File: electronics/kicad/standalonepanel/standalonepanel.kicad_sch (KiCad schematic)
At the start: 106 parts, among them J1 LEDPWR, J2 USB_C-PD, J3 Speaker, Q1 AO4435, SW1 SET, SW2 BOOT, SW3 UP, SW4 DOWN, SW5 TST-ICE40, SW6 RESET, U1 SC189ZSKTRT, U10 DS3231, U2 SC189CSKTRT, U3 CH340C, U4 ESP32-WROVER-E, U5 IS64WV25616EFBLL-10TLI, U6 STUSB4500QTR, U7 ICE40-HX4K, U8 MAX98357A, U9 MPU-6050, X1 12MHz

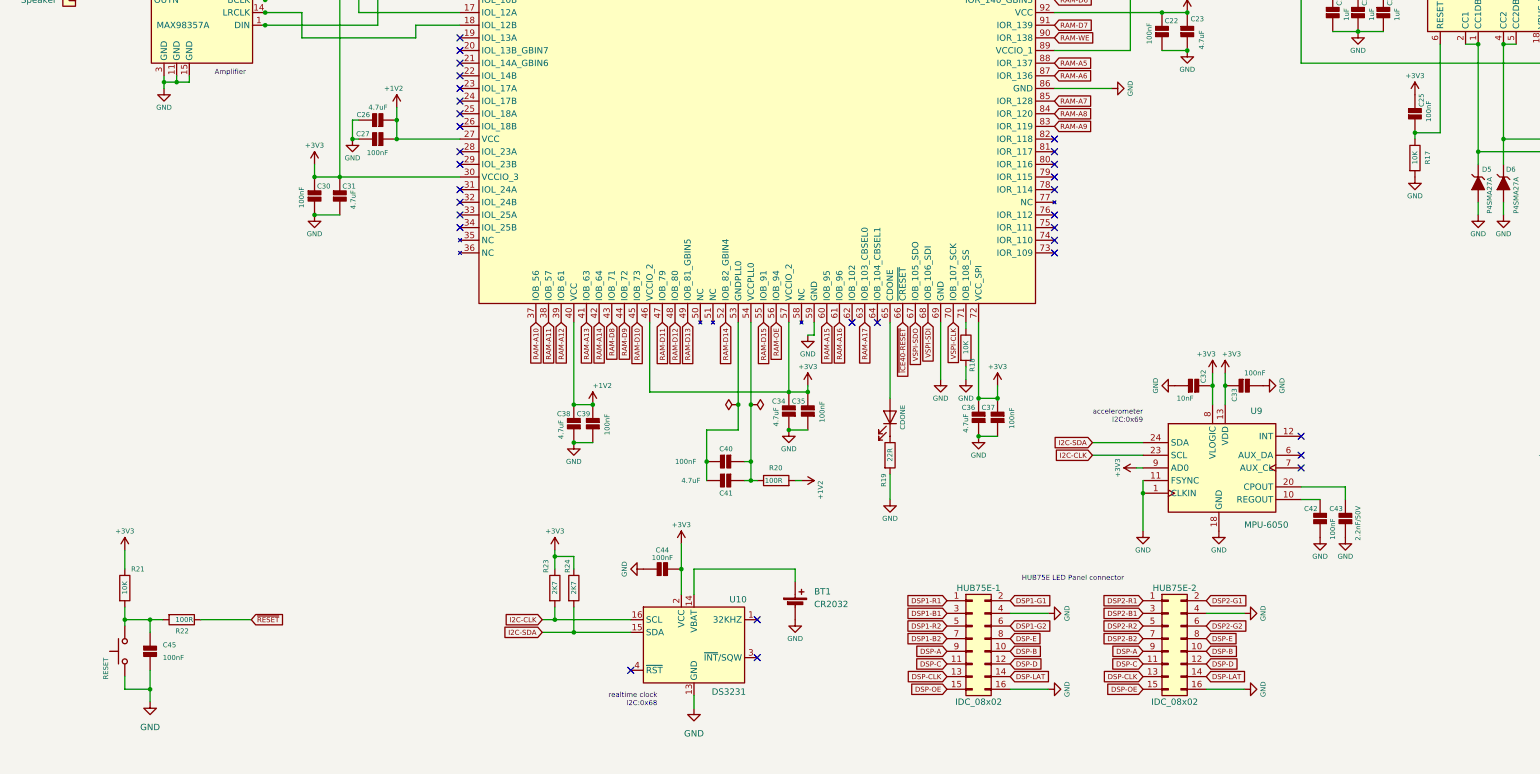
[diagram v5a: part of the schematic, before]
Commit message: added repeat of config selection
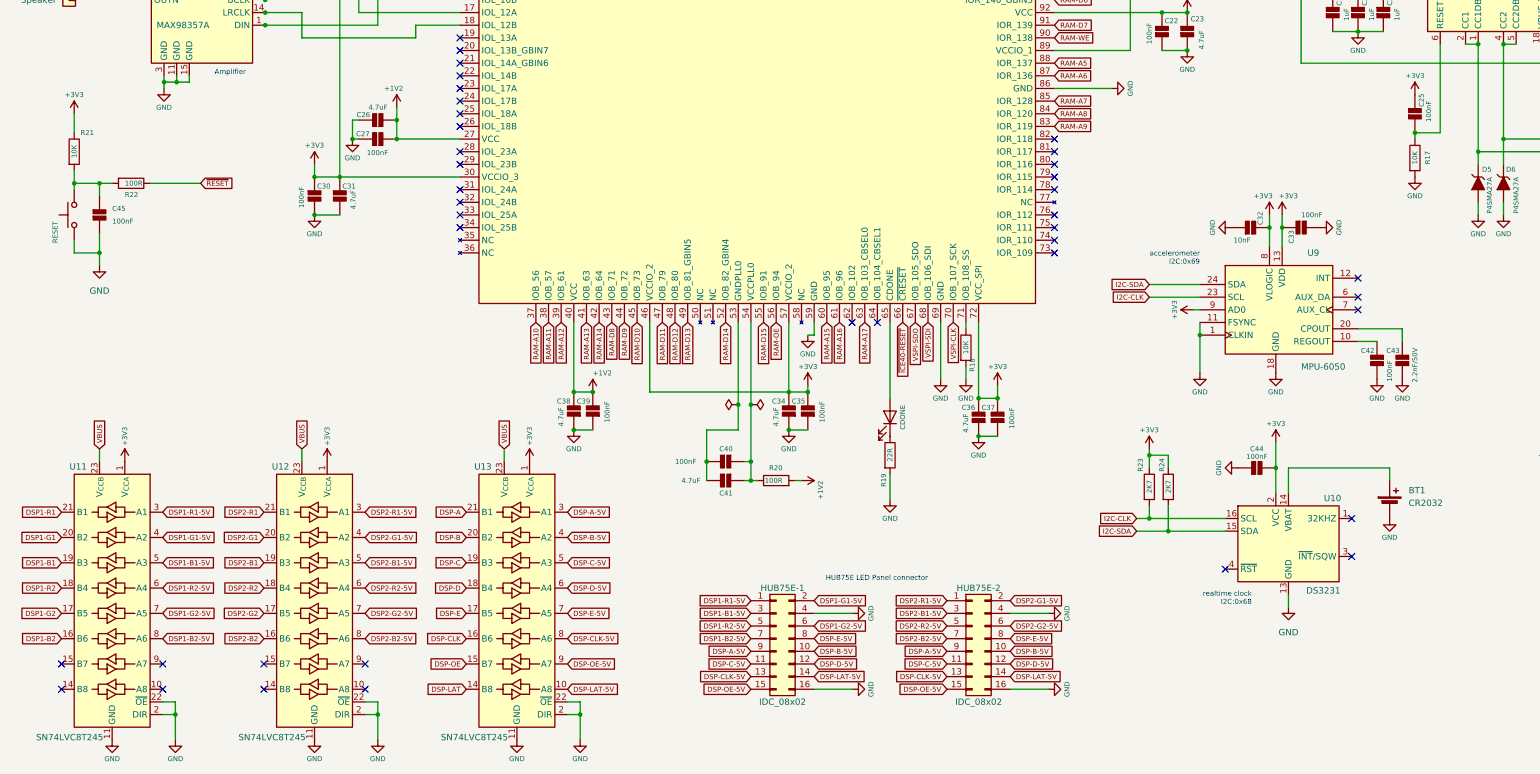
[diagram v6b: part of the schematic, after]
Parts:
- added U11, U12, U13: SN74LVC8T245, Package_SO:TSSOP-24_4.4x7.8mm_P0.65mm, symbol Logic_LevelTranslator:SN74LVC8T245
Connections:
- net +3V3: now also U11.1 (V_{CCA}), U12.1 (V_{CCA}), U13.1 (V_{CCA})
- net DSP-A: now also U13.21 (B1); no longer HUB75E-1.9 (Pin_9), HUB75E-2.9 (Pin_9)
- net DSP-B: now also U13.20 (B2); no longer HUB75E-1.10 (Pin_10), HUB75E-2.10 (Pin_10)
- net DSP-C: now also U13.19 (B3); no longer HUB75E-1.11 (Pin_11), HUB75E-2.11 (Pin_11)
- net DSP-CLK: now also U13.16 (B6); no longer HUB75E-1.13 (Pin_13), HUB75E-2.13 (Pin_13)
- net DSP-D: now also U13.18 (B4); no longer HUB75E-1.12 (Pin_12), HUB75E-2.12 (Pin_12)
- net DSP-E: now also U13.17 (B5); no longer HUB75E-1.8 (Pin_8), HUB75E-2.8 (Pin_8)
- net DSP-LAT: now also U13.14 (B8); no longer HUB75E-1.14 (Pin_14), HUB75E-2.14 (Pin_14)
- net DSP-OE: now also U13.15 (B7); no longer HUB75E-1.15 (Pin_15), HUB75E-2.15 (Pin_15)
- net DSP1-B1: now also U11.19 (B3); no longer HUB75E-1.3 (Pin_3)
- net DSP1-B2: now also U11.16 (B6); no longer HUB75E-1.7 (Pin_7)
- net DSP1-G1: now also U11.20 (B2); no longer HUB75E-1.2 (Pin_2)
- net DSP1-G2: now also U11.17 (B5); no longer HUB75E-1.6 (Pin_6)
- net DSP1-R1: now also U11.21 (B1); no longer HUB75E-1.1 (Pin_1)
- net DSP1-R2: now also U11.18 (B4); no longer HUB75E-1.5 (Pin_5)
- net DSP2-B1: now also U12.19 (B3); no longer HUB75E-2.3 (Pin_3)
- net DSP2-B2: now also U12.16 (B6); no longer HUB75E-2.7 (Pin_7)
- net DSP2-G1: now also U12.20 (B2); no longer HUB75E-2.2 (Pin_2)
- net DSP2-G2: now also U12.17 (B5); no longer HUB75E-2.6 (Pin_6)
- net DSP2-R1: now also U12.21 (B1); no longer HUB75E-2.1 (Pin_1)
- net DSP2-R2: now also U12.18 (B4); no longer HUB75E-2.5 (Pin_5)
- net GND: now also U11.11 (GND), U11.12 (GND), U11.13 (GND), U11.2 (DIR), U11.22 (~{OE}), U12.11 (GND), U12.12 (GND), U12.13 (GND), U12.2 (DIR), U12.22 (~{OE}), U13.11 (GND), U13.12 (GND), U13.13 (GND), U13.2 (DIR), U13.22 (~{OE})
- net VBUS: now also U11.23 (V_{CCB}), U11.24 (V_{CCB}), U12.23 (V_{CCB}), U12.24 (V_{CCB}), U13.23 (V_{CCB}), U13.24 (V_{CCB})
- new net DSP-A-5V: HUB75E-1.9 (Pin_9), HUB75E-2.9 (Pin_9), U13.3 (A1)
- new net DSP-B-5V: HUB75E-1.10 (Pin_10), HUB75E-2.10 (Pin_10), U13.4 (A2)
- new net DSP-C-5V: HUB75E-1.11 (Pin_11), HUB75E-2.11 (Pin_11), U13.5 (A3)
- new net DSP-CLK-5V: HUB75E-1.13 (Pin_13), HUB75E-2.13 (Pin_13), U13.8 (A6)
- new net DSP-D-5V: HUB75E-1.12 (Pin_12), HUB75E-2.12 (Pin_12), U13.6 (A4)
- new net DSP-E-5V: HUB75E-1.8 (Pin_8), HUB75E-2.8 (Pin_8), U13.7 (A5)
- new net DSP-LAT-5V: HUB75E-1.14 (Pin_14), HUB75E-2.14 (Pin_14), U13.10 (A8)
- new net DSP-OE-5V: HUB75E-1.15 (Pin_15), HUB75E-2.15 (Pin_15), U13.9 (A7)
- new net DSP1-B1-5V: HUB75E-1.3 (Pin_3), U11.5 (A3)
- new net DSP1-B2-5V: HUB75E-1.7 (Pin_7), U11.8 (A6)
- new net DSP1-G1-5V: HUB75E-1.2 (Pin_2), U11.4 (A2)
- new net DSP1-G2-5V: HUB75E-1.6 (Pin_6), U11.7 (A5)
- new net DSP1-R1-5V: HUB75E-1.1 (Pin_1), U11.3 (A1)
- new net DSP1-R2-5V: HUB75E-1.5 (Pin_5), U11.6 (A4)
- new net DSP2-B1-5V: HUB75E-2.3 (Pin_3), U12.5 (A3)
- new net DSP2-B2-5V: HUB75E-2.7 (Pin_7), U12.8 (A6)
- new net DSP2-G1-5V: HUB75E-2.2 (Pin_2), U12.4 (A2)
- new net DSP2-G2-5V: HUB75E-2.6 (Pin_6), U12.7 (A5)
- new net DSP2-R1-5V: HUB75E-2.1 (Pin_1), U12.3 (A1)
- new net DSP2-R2-5V: HUB75E-2.5 (Pin_5), U12.6 (A4)
- no-connect marks 78 -> 86
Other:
- moved on the sheet: BT1, C32, C33, C38, C39, C42, C43, C44, C45, HUB75E-1, HUB75E-2, R21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

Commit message: v3 of electronics
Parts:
- removed C14, C25: 100nF, Capacitor_SMD:C_0805_2012Metric_Pad1.18x1.45mm_HandSolder, symbol 0_project:C
- removed C15, C16, C19, C20, C21: 1uF, Capacitor_SMD:C_0805_2012Metric_Pad1.18x1.45mm_HandSolder, symbol 0_project:C
- removed D1, D4, D5, D6: P4SMA27A, Diode_SMD:D_SMA_Handsoldering, symbol 0_project:P4SMA27A
- removed D3: BAT760, Diode_SMD:D_SOD-323, symbol Diode:1N5819WS
- removed LED4: PD, LED_SMD:LED_1206_3216Metric_Pad1.42x1.75mm_HandSolder, symbol Device:LED
- removed Q1: AO4435, Package_SO:SOIC-8_3.9x4.9mm_P1.27mm, symbol 0_project:AO4435
- removed R14: 22K, Resistor_SMD:R_1206_3216Metric_Pad1.30x1.75mm_HandSolder, symbol Device:R
- removed R15: 1K, Resistor_SMD:R_1206_3216Metric_Pad1.30x1.75mm_HandSolder, symbol Device:R
- removed R16: 1K5, Resistor_SMD:R_1206_3216Metric_Pad1.30x1.75mm_HandSolder, symbol Device:R
- removed R17: 10K, Resistor_SMD:R_1206_3216Metric_Pad1.30x1.75mm_HandSolder, symbol Device:R
- removed U6: STUSB4500QTR, 0_project:QFN-24-1EP_4x4mm_P0.5mm_EP2.7x2.7mm, symbol 0_project:STUSB4500QTR
- removed U8: MAX98357A, Package_DFN_QFN:TQFN-16-1EP_3x3mm_P0.5mm_EP1.6x1.6mm, symbol 0_project:MAX98357A
- removed U9: MPU-6050, 0_project:InvenSense_QFN-24_4x4mm_P0.5mm, symbol 0_project:MPU-6050
- added C14: 470uF, Capacitor_SMD:C_Elec_8x10.2, symbol Device:C_Polarized
- added C46, C47: 100nF, Capacitor_SMD:C_0805_2012Metric_Pad1.18x1.45mm_HandSolder, symbol 0_project:C
- added J4: Conn_01x07_Pin, Connector_PinHeader_2.54mm:PinHeader_1x07_P2.54mm_Vertical, symbol Connector:Conn_01x07_Pin
- added JP1: 3V3, Jumper:SolderJumper-2_P1.3mm_Open_RoundedPad1.0x1.5mm, symbol Jumper:SolderJumper_2_Open
- added JP2: 1V2, Jumper:SolderJumper-2_P1.3mm_Open_RoundedPad1.0x1.5mm, symbol Jumper:SolderJumper_2_Open
- added U6: MAX98357A, Package_DFN_QFN:TQFN-16-1EP_3x3mm_P0.5mm_EP1.6x1.6mm, symbol 0_project:MAX98357A
- BT1: footprint 0_project:cr2032_smd_clip -> 0_whitemagic:cr2032_smd_clip
- C28: value 10uF -> 100nF
- C29: value 100nF -> 10uF
- C32: value 10nF -> 100nF
- C43: value 2.2nF/50V -> 100nF
- HUB75E-1, HUB75E-2: footprint 0_project:IDC-Header_2x08_P2.54mm_Horizontal -> 0_whitemagic:IDC-Header_2x08_P2.54mm_Horizontal
- J1: footprint 0_project:JST_VH_1x04_P3.96mm_Horizontal -> 0_whitemagic:JST_VH_1x04_P3.96mm_Horizontal
- J2: footprint 0_project:USB_C_Receptacle_G-Switch_GT-USB-7010ASV -> 0_whitemagic:USB_C_Receptacle_G-Switch_GT-USB-7010ASV
- L1, L2: footprint 0_project:Inductor-040420 -> 0_whitemagic:Inductor-040420
- R10: value 100K -> 390R
- R11: value 1K -> 390R
- R12: value 100R -> 4K7
- R13: value 470R -> 4K7
- SW1: value SET -> UP; footprint 0_project:SW_Tactile_SKHH_Angled -> 0_whitemagic:SW_Tactile_SKHH_Angled
- SW3: value UP -> SET; footprint 0_project:SW_Tactile_SKHH_Angled -> 0_whitemagic:SW_Tactile_SKHH_Angled
- SW4: footprint 0_project:SW_Tactile_SKHH_Angled -> 0_whitemagic:SW_Tactile_SKHH_Angled
- U1, U2: footprint 0_project:SOT23-5-SC189_SEM -> 0_whitemagic:SOT23-5-SC189_SEM
- U4: footprint 0_project:ESP32-WROVER-E -> 0_whitemagic:ESP32-WROVER-E
- X1: footprint 0_project:Oscillator_SMD_EuroQuartz_XO91-4Pin_7.0x5.0mm_HandSoldering -> 0_whitemagic:Oscillator_SMD_EuroQuartz_XO91-4Pin_7.0x5.0mm_HandSoldering
- renumbered R5 to R2, R2 to R5
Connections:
- net +1V2: now also JP2.2 (B); no longer C6.1, L2.2, U2.4 (VOUT)
- net +3V3: now also C42.2, U11.23 (V_{CCB}), U11.24 (V_{CCB}), U12.23 (V_{CCB}), U12.24 (V_{CCB}), U13.23 (V_{CCB}), U13.24 (V_{CCB}), C46.2, J4.1 (Pin_1), JP1.2 (B), U6.7 (VDD), U6.8 (VDD); no longer C32.2, C4.1, L1.2, R1.2, U1.4 (VOUT), U11.1 (V_{CCA}), U12.1 (V_{CCA}), U13.1 (V_{CCA})
- net DSP-A: now also U13.15 (B7); no longer U13.21 (B1)
- net DSP-A-5V: now also U13.9 (A7); no longer U13.3 (A1)
- net DSP-B: now also U13.16 (B6); no longer U13.20 (B2)
- net DSP-B-5V: now also U13.8 (A6); no longer U13.4 (A2)
- net DSP-C: now also U13.17 (B5); no longer U13.19 (B3)
- net DSP-C-5V: now also U13.7 (A5); no longer U13.5 (A3)
- net DSP-CLK: now also U13.19 (B3); no longer U13.16 (B6)
- net DSP-CLK-5V: now also U13.5 (A3); no longer U13.8 (A6)
- net DSP-E: now also U13.14 (B8), U7.125 (IOT_192); no longer U13.17 (B5), U7.124 (IOT_191)
- net DSP-E-5V: now also U13.10 (A8); no longer U13.7 (A5)
- net DSP-LAT: now also U13.20 (B2); no longer U13.14 (B8)
- net DSP-LAT-5V: now also U13.4 (A2); no longer U13.10 (A8)
- net DSP-OE: now also U13.21 (B1); no longer U13.15 (B7)
- net DSP-OE-5V: now also U13.3 (A1); no longer U13.9 (A7)
- net DSP1-B2: now also U7.124 (IOT_191); no longer U7.125 (IOT_192)
- net GND: now also C32.2, C43.2, R12.1, R13.1, C14.2, C46.1, C47.2, J4.7 (Pin_7), U6.11 (GND), U6.15 (GND), U6.2 (GAIN_SLOT), U6.3 (GND); no longer C32.1, C43.1
- net I2C-CLK: now also J4.3 (Pin_3)
- net I2C-SDA: now also J4.2 (Pin_2)
- net VBUS: now also C32.1, C43.1, J1.1 (Pin_1), J1.2 (Pin_2), U11.1 (V_{CCA}), U12.1 (V_{CCA}), U13.1 (V_{CCA}), C14.1, C47.1; no longer R10.1, R13.1, U11.23 (V_{CCB}), U11.24 (V_{CCB}), U12.23 (V_{CCB}), U12.24 (V_{CCB}), U13.23 (V_{CCB}), U13.24 (V_{CCB})
- net VSPI-CLK: now also J4.4 (Pin_4)
- net VSPI-SDI: now also J4.5 (Pin_5)
- net VSPI-SDO: now also J4.6 (Pin_6)
- net at R10.2: now also J2.B5 (CC2); no longer R12.2
- net at LED3.2 (A): now also U7.7 (IOL_4A); no longer U7.144 (IOT_222)
- net at J2.A5 (CC1): now also R11.2
- net at R13.2: now also R10.1
- net at J3.1 (Pin_1): now also U6.9 (OUTP)
- net at J3.2 (Pin_2): now also U6.10 (OUTN)
- net at U7.1 (IOL_2A): now also U6.4 (~{SD_MODE})
- net at U7.2 (IOL_2B): now also U6.1 (DIN)
- net at U7.3 (IOL_3A): now also U6.16 (BCLK)
- net at U7.4 (IOL_3B): now also U6.14 (LRCLK)
- removed net VPANEL: J1.1 (Pin_1), J1.2 (Pin_2), R11.1
- new net: C4.1, JP1.1 (A), L1.2, R1.2, U1.4 (VOUT)
- new net: C6.1, JP2.1 (A), L2.2, U2.4 (VOUT)
- new net: R11.1, R12.2
- no-connect marks 86 -> 78
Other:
- note added: "resistors (~5K1) enable 5V/3A on USB-C 1.2"
- note removed: "USB PD Sink I2C:0x28"
- note removed: "accelerometer I2C:0x69"
- company: (none) -> White Magic
- title: (none) -> Standalone Panel
- moved on the sheet: BT1, C24, C28, C29, C3, C4, C44, C5, C6, J3, L1, L2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
